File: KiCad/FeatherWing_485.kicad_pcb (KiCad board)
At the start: 2 copper layers, 50.8 x 22.9 mm, 17 parts, among them J1 feather long, J2 feather short, J3 Screw_Terminal_01x03, Q1 BC857, U1 MAX3485

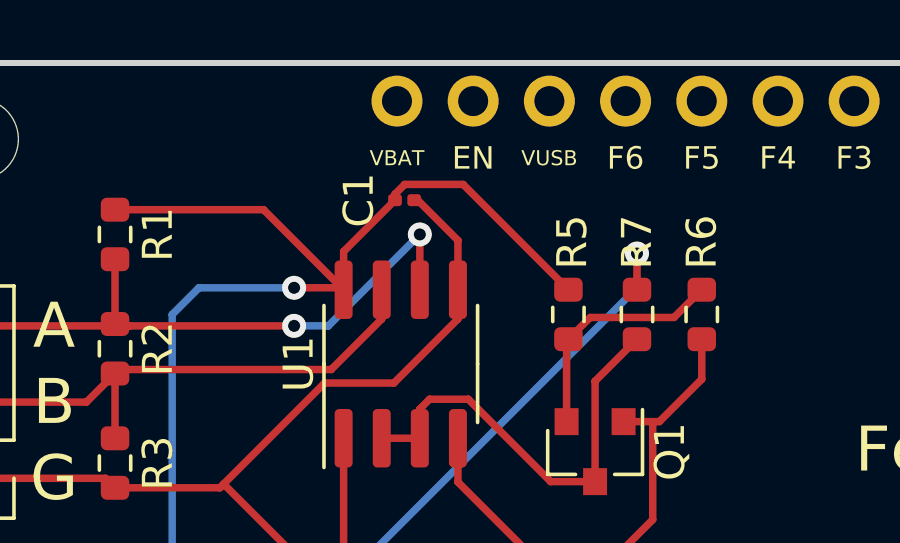
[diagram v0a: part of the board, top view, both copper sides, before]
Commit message: Fix footprint
Use 0603 footprint for C1
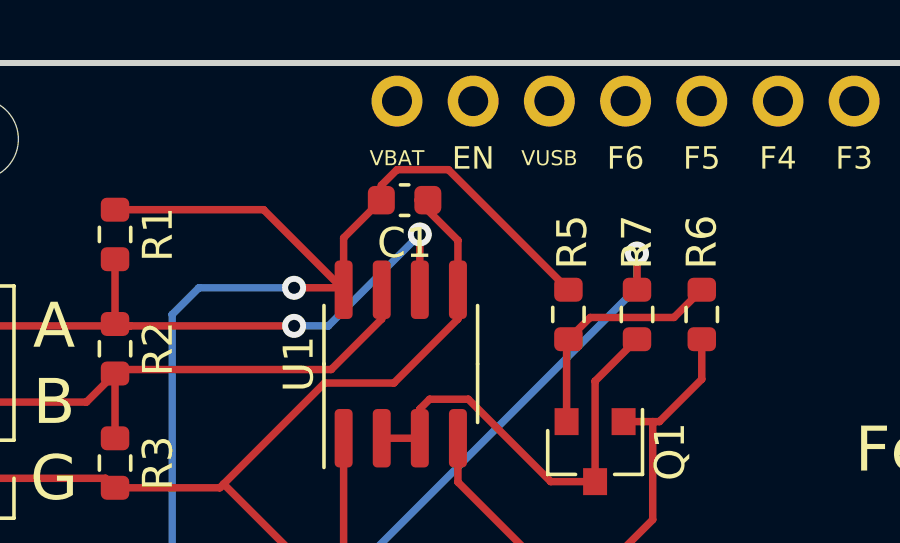
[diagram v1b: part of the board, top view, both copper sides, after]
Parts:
- C1: footprint Capacitor_SMD:C_0201_0603Metric -> Capacitor_SMD:C_0603_1608Metric
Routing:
- net +3V3: track 39.4 -> 40.2 mm

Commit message: Updated PCB
Add copper fill.
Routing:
- net GND: vias 2 -> 8
- added copper zone on B.Cu, net GND
- added copper zone on F.Cu, net GND

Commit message: Update kicad files
Update for revised PCB
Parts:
- added J4: Conn_01x03_Male, Connector_PinHeader_2.54mm:PinHeader_1x03_P2.54mm_Vertical, F.Cu at (27.1, 39.1)
- added OSHW_Mono_0.1_Scale: US001031, KiCad:OSHW_Mono_0.1_Scale, F.Cu at (53.8, 40.1)
- added REF**: OSHW-Logo2_7.3x6mm_SilkScreen, Symbol:OSHW-Logo2_7.3x6mm_SilkScreen, F.Cu at (45.6, 40.5)
- added U2: TVS0500DRV, Package_SON:WSON-6-1EP_2x2mm_P0.65mm_EP1x1.6mm, F.Cu at (36.8, 32.4)
- added U3: TVS0500DRV, Package_SON:WSON-6-1EP_2x2mm_P0.65mm_EP1x1.6mm, F.Cu at (36.8, 37.7)
- J3: footprint Connector_PinHeader_2.54mm:PinHeader_1x03_P2.54mm_Vertical -> Connector_Phoenix_MC:PhoenixContact_MCV_1,5_3-G-3.5_1x03_P3.50mm_Vertical
- moved R1 37.1 mm to (69.6, 33.0), turned to 180 degrees
- moved R3 29.1 mm to (61.6, 37.1), turned to 180 degrees
- moved R5 26.5 mm to (73.9, 37.0), turned to 0 degrees
- moved R4 24.9 mm to (73.2, 41.0), turned to 90 degrees
- moved U1 24.7 mm to (66.2, 40.5)
- moved R6 23.7 mm to (74.7, 41.0), turned to 270 degrees
- moved C1 22.7 mm to (62.1, 40.8), turned to 90 degrees
- moved Q1 22.2 mm to (70.6, 40.8), turned to 90 degrees
- moved R7 20.8 mm to (70.5, 37.0), turned to 180 degrees
- moved R2 6.48 mm to (39.0, 35.1)
- moved J3 2.74 mm to (30.4, 40.3), turned to 90 degrees
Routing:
- net GND: track 49.3 -> 13.8 mm, vias 8 -> 7
- net Net-(J3-Pad2): track 17.9 -> 45.6 mm, vias 0 -> 2
- net Net-(J3-Pad3): track 20.7 -> 48.2 mm
- net /RX: track 31.0 -> 4.21 mm
- net /TX: track 28.0 -> 9.87 mm
- net +3V3: track 40.2 -> 50.0 mm, vias 2 -> 0
- net Net-(Q1-Pad3): track 14.7 -> 10.1 mm
- net Net-(Q1-Pad1): track 10.0 -> 5.96 mm
- net Net-(Q1-Pad2): track 7.90 -> 9.20 mm
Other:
- board text removed: "A0"
- board text removed: "A1"
- board text removed: "A2"
- board text removed: "A3"
- board text removed: "A4"
- board text removed: "A5"
- board text removed: "AREF"
- board text removed: "EN"
- board text removed: "F0"
- board text removed: "F1"
- board text removed: "F2"
- board text removed: "F3"
- board text removed: "F4"
- board text removed: "F5"
- board text removed: "F6"
- board text removed: "FREE"
- board text removed: "MISO"
- board text removed: "MOSI"
- board text removed: "SCK"
- board text removed: "SCL"
- board text removed: "SDA"
- board text removed: "VBAT"
- board text removed: "VUSB"
- board text removed: "~RST"
